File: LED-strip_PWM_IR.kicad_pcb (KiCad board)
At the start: 2 copper layers, 32 x 16 mm, 20 parts, among them IC1 ATTINY85-S, P1 CONN_2, P2 CONN_2, Q1 8MHz, T1 IRLR2905_DPAK, U1 TSOP38238, U2 MCP1804-SOT23-5

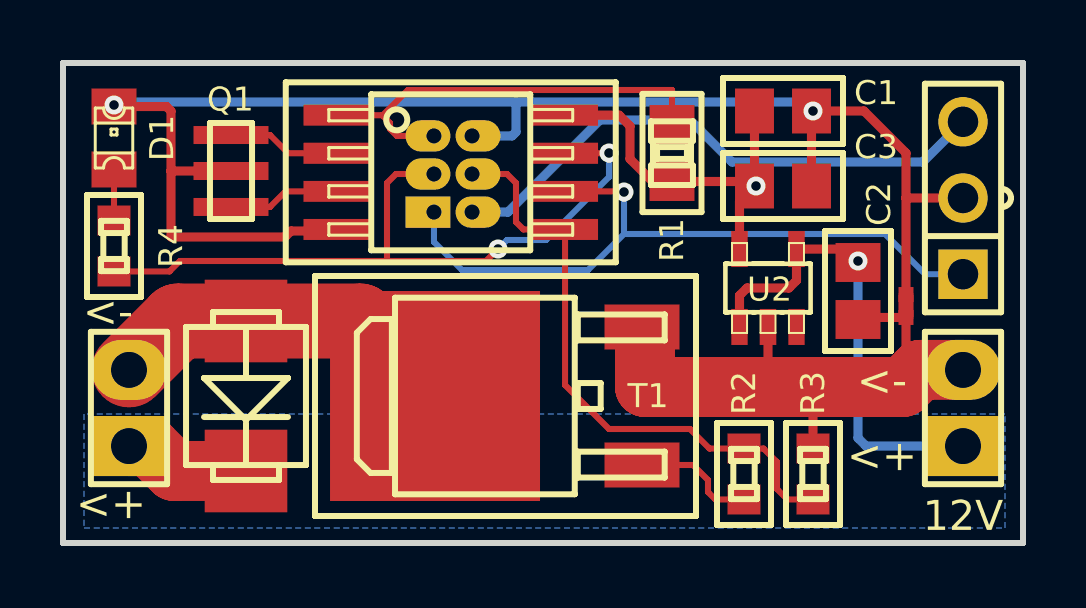
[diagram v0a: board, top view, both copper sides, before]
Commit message: Added heat-sink copper-pour with lots of vias again. Board-Rev. 0.42
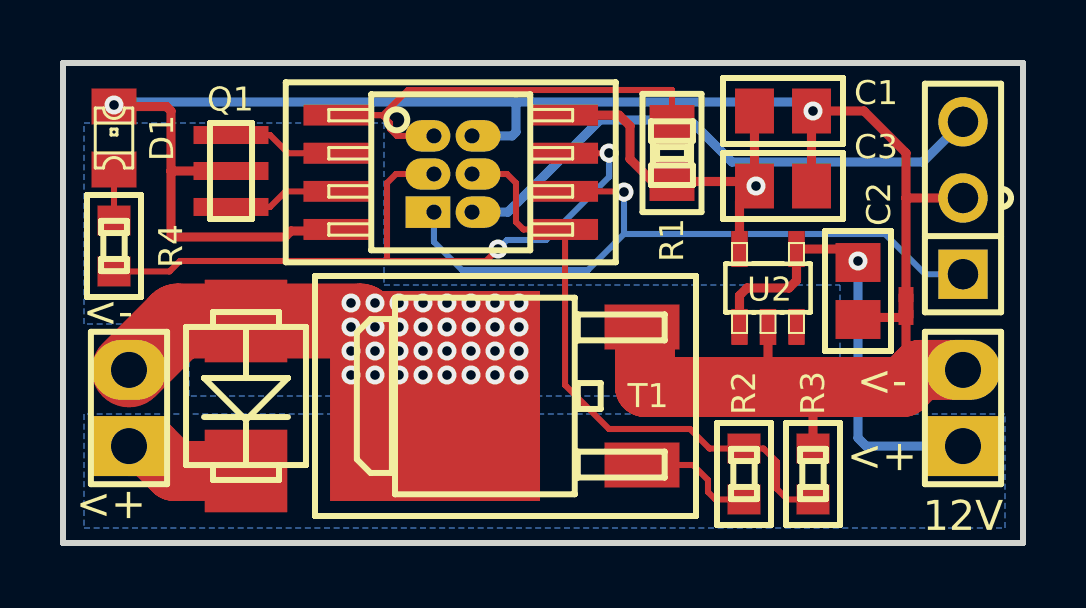
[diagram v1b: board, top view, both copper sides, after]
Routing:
- net /drain: track 11.9 -> 41.4 mm, vias 0 -> 32
- added copper zone on B.Cu, net /drain
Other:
- board text added: "V0.42 IR PWM controller"
- board text removed: "V0.41 IR PWM controller"
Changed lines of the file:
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@@
-(kicad_pcb (version 3) (host pcbnew "(2013-05-18 BZR 4155)-testing")
+(kicad_pcb (version 3) (host pcbnew "(2013-05-24 BZR 4163)-testing")
   (general
     (links 38)
@@
     (thickness 1.6002)
     (drawings 19)
-    (tracks 144)
+    (tracks 213)
     (zones 0)
     (modules 20)
@@
   (title_block
     (title LED-strip_PWM_IR)
-    (rev 0.41)
+    (rev 0.42)
     (company "2012 - blog.spitzenpfeil.org")
   )
@@
     (user_trace_width 2.5)
     (trace_clearance 0.2032)
-    (zone_clearance 0.2)
+    (zone_clearance 0.25)
     (zone_45_only yes)
     (trace_min 0.1524)
@@
     (effects (font (size 1 1) (thickness 0.2)))
   )
-  (gr_text "V0.41\nIR PWM controller" (at 91 50.8) (layer B.SilkS)
+  (gr_text "V0.42\nIR PWM controller" (at 91 50.8) (layer B.SilkS)
     (effects (font (size 1.016 1.016) (thickness 0.2032)) (justify mirror))
   )
@@
   (segment (start 79.9 48.6) (end 86.8 48.6) (width 0.2032) (layer Front) (net 4))
   (segment (start 77.7 48.94836) (end 79.55164 48.94836) (width 0.2032) (layer Front) (net 4) (status 10))
-  (segment (start 78.2 54.77) (end 78.87 54.77) (width 2) (layer Front) (net 5))
-  (segment (start 79.69936 55.59936) (end 82.1 55.59936) (width 2) (layer Front) (net 5))
-  (segment (start 78.87 54.77) (end 79.69936 55.59936) (width 2) (layer Front) (net 5))
+  (segment (start 78.2 54.77) (end 78.87 54.77) (width 2) (layer Front) (net 5) (status 30))
+  (segment (start 79.69936 55.59936) (end 82.1 55.59936) (width 2) (layer Front) (net 5) (status 20))
+  (segment (start 78.87 54.77) (end 79.69936 55.59936) (width 2) (layer Front) (net 5) (status 10))
   (segment (start 102.5 54.5) (end 102.5 48.6) (width 0.3048) (layer Back) (net 5))
   (segment (start 106 54.77) (end 102.77 54.77) (width 0.3048) (layer Back) (net 5) (status 10))
@@
   (segment (start 83.4212 46.2788) (end 85.1154 46.2788) (width 0.2032) (layer Front) (net 7) (status 20))
   (segment (start 82.90112 46.79888) (end 83.4212 46.2788) (width 0.2032) (layer Front) (net 7))
+  (segment (start 85.6 50) (end 85.6 50.8) (width 0.2032) (layer Back) (net 8))
+  (segment (start 85.5 52.3) (end 85.6 52.4) (width 0.2032) (layer Back) (net 8))
+  (via (at 85.6 52.4) (size 0.635) (layers Front Back) (net 8) (status 30))
+  (segment (start 85.6 52.4) (end 86.4 52.4) (width 0.2032) (layer Front) (net 8) (status 30))
+  (via (at 86.4 52.4) (size 0.635) (layers Front Back) (net 8) (status 30))
+  (segment (start 86.4 52.4) (end 87.2 52.4) (width 0.2032) (layer Back) (net 8))
+  (via (at 87.2 52.4) (size 0.635) (layers Front Back) (net 8) (status 30))
+  (segment (start 87.2 52.4) (end 88 52.4) (width 0.2032) (layer Front) (net 8) (status 30))
+  (via (at 88 52.4) (size 0.635) (layers Front Back) (net 8) (status 30))
+  (segment (start 88 52.4) (end 88.8 52.4) (width 0.2032) (layer Back) (net 8))
+  (via (at 88.8 52.4) (size 0.635) (layers Front Back) (net 8) (status 30))
+  (segment (start 88.8 52.4) (end 89.6 52.4) (width 0.2032) (layer Front) (net 8) (status 30))
+  (via (at 89.6 52.4) (size 0.635) (layers Front Back) (net 8) (status 30))
+  (segment (start 89.6 52.4) (end 90.4 52.4) (width 0.2032) (layer Back) (net 8))
+  (via (at 90.4 52.4) (size 0.635) (layers Front Back) (net 8) (status 30))
+  (segment (start 90.4 52.4) (end 91.2 52.4) (width 0.2032) (layer Front) (net 8) (status 30))
+  (via (at 91.2 52.4) (size 0.635) (layers Front Back) (net 8) (status 30))
+  (segment (start 91.2 52.4) (end 91.2 51.6) (width 0.2032) (layer Back) (net 8))
+  (via (at 91.2 51.6) (size 0.635) (layers Front Back) (net 8) (status 30))
+  (segment (start 91.2 51.6) (end 91.2 50.8) (width 0.2032) (layer Front) (net 8) (status 30))
+  (via (at 91.2 50.8) (size 0.635) (layers Front Back) (net 8) (status 30))
+  (segment (start 91.2 50.8) (end 91.2 50) (width 0.2032) (layer Back) (net 8))
+  (via (at 91.2 50) (size 0.635) (layers Front Back) (net 8) (status 30))
+  (segment (start 91.2 50) (end 90.4 50) (width 0.2032) (layer Front) (net 8) (status 30))
+  (via (at 90.4 50) (size 0.635) (layers Front Back) (net 8) (status 30))
+  (segment (start 90.4 50) (end 89.6 50) (width 0.2032) (layer Back) (net 8))
+  (via (at 89.6 50) (size 0.635) (layers Front Back) (net 8) (status 30))
+  (segment (start 89.6 50) (end 88.8 50) (width 0.2032) (layer Front) (net 8) (status 30))
+  (via (at 88.8 50) (size 0.635) (layers Front Back) (net 8) (status 30))
+  (segment (start 88.8 50) (end 88 50) (width 0.2032) (layer Back) (net 8))
+  (via (at 88 50) (size 0.635) (layers Front Back) (net 8) (status 30))
+  (segment (start 88 50) (end 87.2 50) (width 0.2032) (layer Front) (net 8) (status 30))
+  (via (at 87.2 50) (size 0.635) (layers Front Back) (net 8) (status 30))
+  (segment (start 87.2 50) (end 86.4 50) (width 0.2032) (layer Back) (net 8))
+  (via (at 86.4 50) (size 0.635) (layers Front Back) (net 8) (status 30))
+  (segment (start 86.4 50) (end 85.6 50) (width 0.2032) (layer Front) (net 8) (status 30))
+  (via (at 85.6 50) (size 0.635) (layers Front Back) (net 8) (status 30))
+  (segment (start 85.5 50.3) (end 85.5 52.3) (width 0.2032) (layer Back) (net 8))
+  (via (at 90.4 51.6) (size 0.635) (layers Front Back) (net 8) (status 30))
+  (segment (start 90.4 50.8) (end 90.4 51.6) (width 0.2032) (layer Front) (net 8) (status 30))
+  (via (at 90.4 50.8) (size 0.635) (layers Front Back) (net 8) (status 30))
+  (segment (start 89.6 50.8) (end 90.4 50.8) (width 0.2032) (layer Back) (net 8))
+  (via (at 89.6 50.8) (size 0.635) (layers Front Back) (net 8) (status 30))
+  (segment (start 89.6 51.6) (end 89.6 50.8) (width 0.2032) (layer Front) (net 8) (status 30))
+  (via (at 89.6 51.6) (size 0.635) (layers Front Back) (net 8) (status 30))
+  (segment (start 88.8 51.6) (end 89.6 51.6) (width 0.2032) (layer Back) (net 8))
+  (via (at 88.8 51.6) (size 0.635) (layers Front Back) (net 8) (status 30))
+  (segment (start 88.8 50.8) (end 88.8 51.6) (width 0.2032) (layer Front) (net 8) (status 30))
+  (via (at 88.8 50.8) (size 0.635) (layers Front Back) (net 8) (status 30))
+  (segment (start 88 50.8) (end 88.8 50.8) (width 0.2032) (layer Back) (net 8))
+  (via (at 88 50.8) (size 0.635) (layers Front Back) (net 8) (status 30))
+  (segment (start 88 51.6) (end 88 50.8) (width 0.2032) (layer Front) (net 8) (status 30))
+  (via (at 88 51.6) (size 0.635) (layers Front Back) (net 8) (status 30))
+  (segment (start 87.2 51.6) (end 88 51.6) (width 0.2032) (layer Back) (net 8))
+  (via (at 87.2 51.6) (size 0.635) (layers Front Back) (net 8) (status 30))
+  (segment (start 87.2 50.8) (end 87.2 51.6) (width 0.2032) (layer Front) (net 8) (status 30))
+  (via (at 87.2 50.8) (size 0.635) (layers Front Back) (net 8) (status 30))
+  (segment (start 86.4 50.8) (end 87.2 50.8) (width 0.2032) (layer Back) (net 8))
+  (via (at 86.4 50.8) (size 0.635) (layers Front Back) (net 8) (status 30))
+  (segment (start 86.4 51.6) (end 86.4 50.8) (width 0.2032) (layer Front) (net 8) (status 30))
+  (via (at 86.4 51.6) (size 0.635) (layers Front Back) (net 8) (status 30))
+  (segment (start 85.6 51.6) (end 86.4 51.6) (width 0.2032) (layer Back) (net 8))
+  (via (at 85.6 51.6) (size 0.635) (layers Front Back) (net 8) (status 30))
+  (segment (start 85.6 50.8) (end 85.6 51.6) (width 0.2032) (layer Front) (net 8) (status 30))
+  (via (at 85.6 50.8) (size 0.635) (layers Front Back) (net 8) (status 30))
+  (segment (start 78.2 52.23) (end 78.37 52.23) (width 0.2032) (layer Back) (net 8) (status 30))
+  (segment (start 88.7 50.3) (end 89.5 50.3) (width 0.2032) (layer Front) (net 8) (status 30))
+  (segment (start 87.1 50.3) (end 87.9 50.3) (width 0.2032) (layer Front) (net 8) (status 30))
+  (segment (start 85.5 50.3) (end 86.3 50.3) (width 0.2032) (layer Front) (net 8) (status 30))
   (segment (start 79.82936 50.60064) (end 82.1 50.60064) (width 2.5) (layer Front) (net 8) (status 20))
   (segment (start 82.1 50.60064) (end 85.90128 50.60064) (width 2.5) (layer Front) (net 8) (status 30))
@@
   (segment (start 99.1 46.1) (end 99.05004 46.1) (width 0.3048) (layer Front) (net 13) (status 30))
   (via (at 99.1 46.1) (size 0.635) (layers Front Back) (net 13) (status 30))
-  (segment (start 106 43.96) (end 104.66 45.3) (width 0.3048) (layer Back) (net 13))
+  (segment (start 106 43.96) (end 104.66 45.3) (width 0.3048) (layer Back) (net 13) (status 10))
   (segment (start 93.9 43.9) (end 96.9 43.9) (width 0.3048) (layer Back) (net 13))
-  (segment (start 90.83 46.97) (end 89.635 46.97) (width 0.3048) (layer Back) (net 13) (status 10))
+  (segment (start 90.83 46.97) (end 89.635 46.97) (width 0.3048) (layer Back) (net 13) (status 20))
   (segment (start 90.83 46.97) (end 93.9 43.9) (width 0.3048) (layer Back) (net 13))
   (segment (start 96.9 43.9) (end 98.3 45.3) (width 0.3048) (layer Back) (net 13))
@@
       )
     )
+  )
+  (zone (net 8) (net_name /drain) (layer Back) (hatch edge 0.508)
+    (connect_pads (clearance 0.25))
+    (min_thickness 0.25)
+    (fill (arc_segments 16) (thermal_gap 0.25) (thermal_bridge_width 0.499999) (smoothing fillet) (radius 0.5))
+    (polygon
+      (pts
+        (xy 101.9 53.1) (xy 80.2 53.1) (xy 80.2 50.7) (xy 76.7 50.7) (xy 76.7 44)
+        (xy 86.7 44) (xy 86.7 49.4) (xy 101.9 49.4)
+      )
+    )

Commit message: Switched Schottky diode to SS14L + rounded corners.
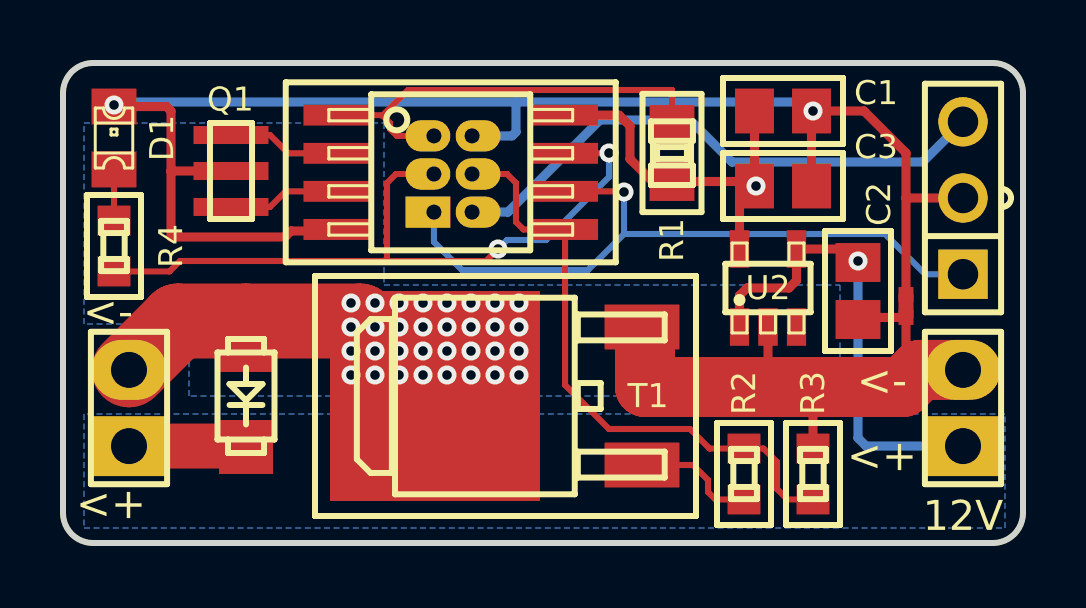
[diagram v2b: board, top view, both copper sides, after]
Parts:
- DS1: value MBRS140T3G -> SS14L; footprint MADW__diode-SMB-package -> MADW__diode_sub-SMA
- U2: footprint -SOT23-5L -> MADW__SOT23-5
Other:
- outline, holes or cut-outs redrawn
- board text added: "V0.43 IR PWM controller"
- board text removed: "V0.42 IR PWM controller"

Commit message: Fixed resonator footprint (library part was off).
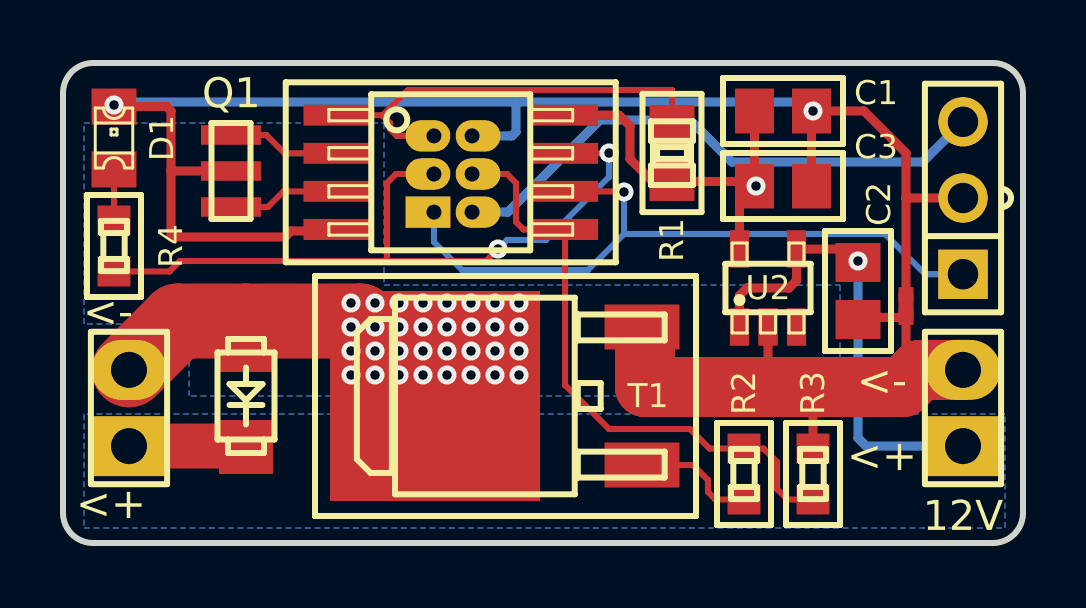
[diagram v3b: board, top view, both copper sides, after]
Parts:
- Q1: value 8MHz -> CSTCE8M00G55-R0; footprint MADW__murata-resonator_CSTCE-G -> MADW__murata-resonator__CSTCE8M00G55-R0
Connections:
- net N-000001 renamed Net-<D1-Pad1>
- net N-000004 renamed Net-<R2-Pad2>
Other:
- board text added: "V0.43.b IR PWM controller"
- board text removed: "V0.43 IR PWM controller"
